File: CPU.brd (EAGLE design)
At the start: 101.6 x 34 mm, 4 parts, among them IC1 Z80CPU

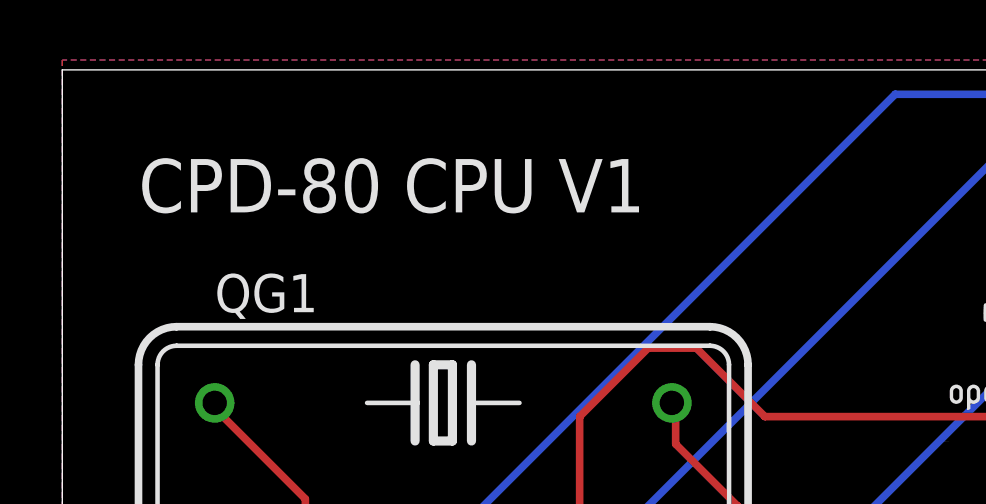
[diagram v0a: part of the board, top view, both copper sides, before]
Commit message: Update names and font
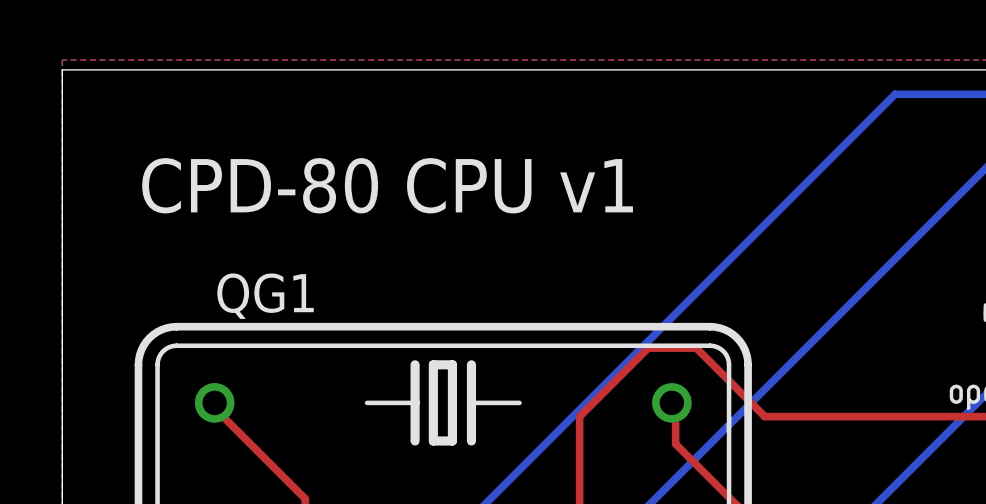
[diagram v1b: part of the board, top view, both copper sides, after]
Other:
- board text added: "CPD-80 CPU v1"
- board text removed: "CPD-80 CPU V1"
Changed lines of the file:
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@@
 <wire x1="102.87" y1="0" x2="102.85" y2="0" width="0.0254" layer="20"/>
 <wire x1="102.85" y1="0" x2="1.27" y2="0" width="0.0254" layer="20"/>
-<text x="3.81" y="29.21" size="1.778" layer="21">CPD-80 CPU V1</text>
+<text x="3.81" y="29.21" size="1.778" layer="21" font="fixed">CPD-80 CPU v1</text>
 <rectangle x1="98.7933" y1="26.7335" x2="99.1235" y2="26.7589" layer="21"/>
 <rectangle x1="98.5901" y1="26.7589" x2="99.1997" y2="26.7843" layer="21"/>

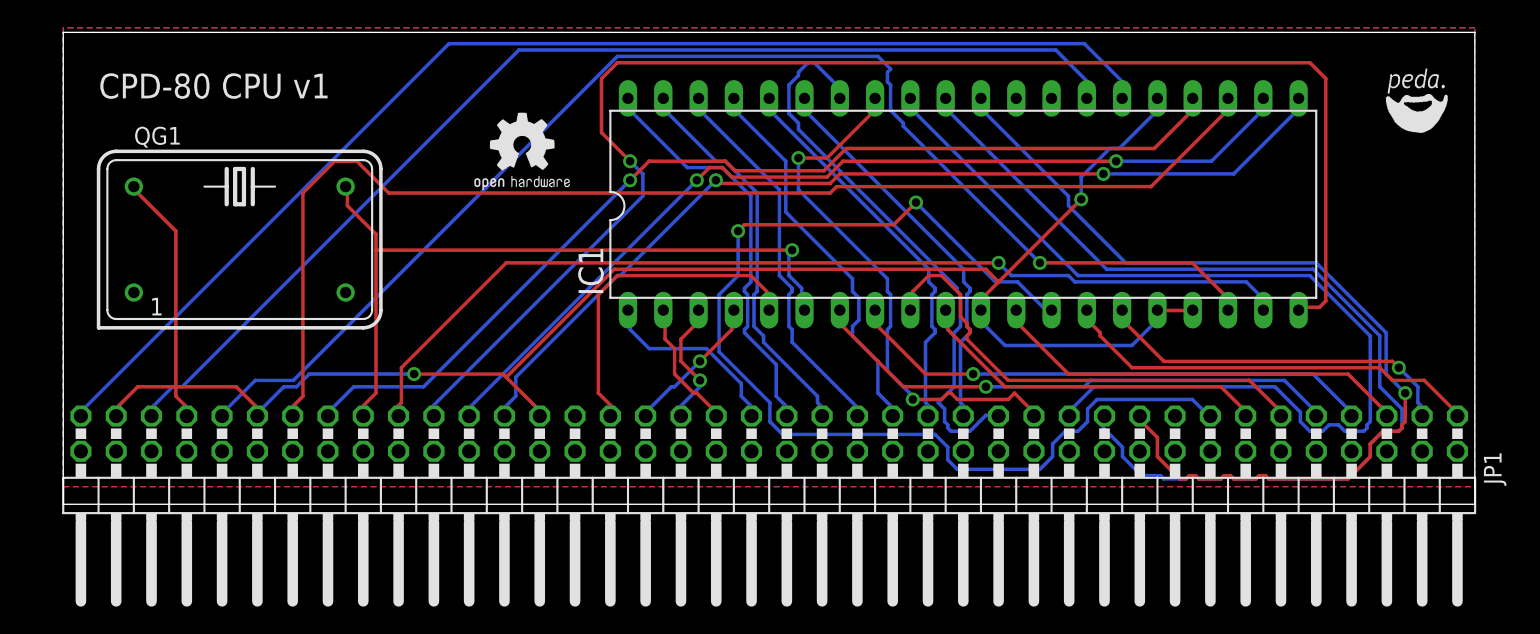
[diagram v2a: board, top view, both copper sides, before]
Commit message: Add Decoupling Capacitors.
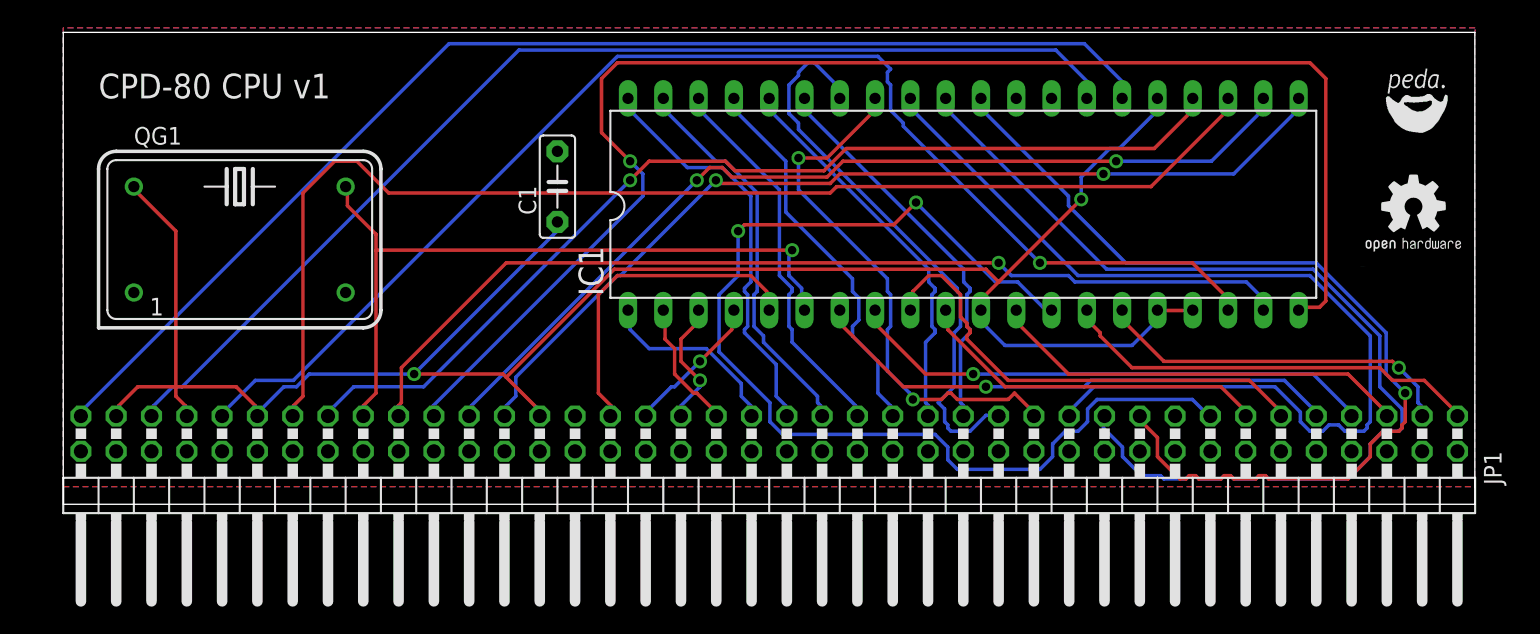
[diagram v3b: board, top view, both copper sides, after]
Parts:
- added C1: 0.1µF, capacitor-wima:C5B2.5
- moved U$1 64.3 mm to (94.6, 17.1)
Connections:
- net GND: now also C1.2
- net VCC: now also C1.1
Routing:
- net VCC: track 132.4 -> 147.6 mm
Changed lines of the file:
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@@
 <attribute name="MF" value="" x="13.97" y="19.05" size="1.778" layer="27" display="off"/>
 </element>
-<element name="U$1" library="bfl" package="OSHW2" value="" x="30.48" y="21.59"/>
+<element name="U$1" library="bfl" package="OSHW2" value="" x="94.615" y="17.145"/>
+<element name="C1" library="capacitor-wima" package="C5B2.5" value="0.1µF" x="36.83" y="22.86" rot="R90"/>
 </elements>
 <signals>
@@
 <via x="74.5236" y="21.9456" extent="1-16" drill="0.6096"/>
 <via x="26.5176" y="9.3726" extent="1-16" drill="0.6096"/>
+<contactref element="C1" pad="1"/>
+<wire x1="36.8046" y1="19.6596" x2="36.8046" y2="20.1168" width="0.254" layer="16"/>
+<wire x1="26.5176" y1="9.3726" x2="36.8046" y2="19.6596" width="0.254" layer="16"/>
+<wire x1="36.8046" y1="20.1168" x2="36.83" y2="20.32" width="0.254" layer="16"/>
 </signal>
 <signal name="GND">
@@
 <vertex x="102.87" y="34.29"/>
 </polygon>
+<contactref element="C1" pad="2"/>
 </signal>
 <signal name="CLOCK">

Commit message: Add Ground Rail to JEANNECTOR
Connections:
- net GND: now also JP1.10, JP1.12, JP1.14, JP1.16, JP1.18, JP1.2, JP1.20, JP1.22, JP1.24, JP1.26, JP1.28, JP1.30, JP1.32, JP1.34, JP1.36, JP1.38, JP1.4, JP1.40, JP1.42, JP1.44, JP1.46, JP1.48, JP1.50, JP1.52, JP1.54, JP1.56, JP1.58, JP1.6, JP1.60, JP1.62, JP1.64, JP1.66, JP1.68, JP1.70, JP1.72, JP1.74, JP1.76, JP1.78, JP1.8, JP1.80
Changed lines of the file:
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@@
 </polygon>
 <contactref element="C1" pad="2"/>
+<contactref element="JP1" pad="2"/>
+<contactref element="JP1" pad="4"/>
+<contactref element="JP1" pad="6"/>
+<contactref element="JP1" pad="8"/>
+<contactref element="JP1" pad="10"/>
+<contactref element="JP1" pad="12"/>
+<contactref element="JP1" pad="14"/>
+<contactref element="JP1" pad="16"/>
+<contactref element="JP1" pad="18"/>
+<contactref element="JP1" pad="20"/>
+<contactref element="JP1" pad="22"/>
+<contactref element="JP1" pad="24"/>
+<contactref element="JP1" pad="26"/>
+<contactref element="JP1" pad="28"/>
+<contactref element="JP1" pad="30"/>
+<contactref element="JP1" pad="32"/>
+<contactref element="JP1" pad="34"/>
+<contactref element="JP1" pad="36"/>
+<contactref element="JP1" pad="38"/>
+<contactref element="JP1" pad="40"/>
+<contactref element="JP1" pad="42"/>
+<contactref element="JP1" pad="44"/>
+<contactref element="JP1" pad="46"/>
+<contactref element="JP1" pad="48"/>
+<contactref element="JP1" pad="50"/>
+<contactref element="JP1" pad="52"/>
+<contactref element="JP1" pad="54"/>
+<contactref element="JP1" pad="56"/>
+<contactref element="JP1" pad="58"/>
+<contactref element="JP1" pad="60"/>
+<contactref element="JP1" pad="62"/>
+<contactref element="JP1" pad="64"/>
+<contactref element="JP1" pad="66"/>
+<contactref element="JP1" pad="68"/>
+<contactref element="JP1" pad="70"/>
+<contactref element="JP1" pad="72"/>
+<contactref element="JP1" pad="74"/>
+<contactref element="JP1" pad="76"/>
+<contactref element="JP1" pad="78"/>
+<contactref element="JP1" pad="80"/>
 </signal>
 <signal name="CLOCK">

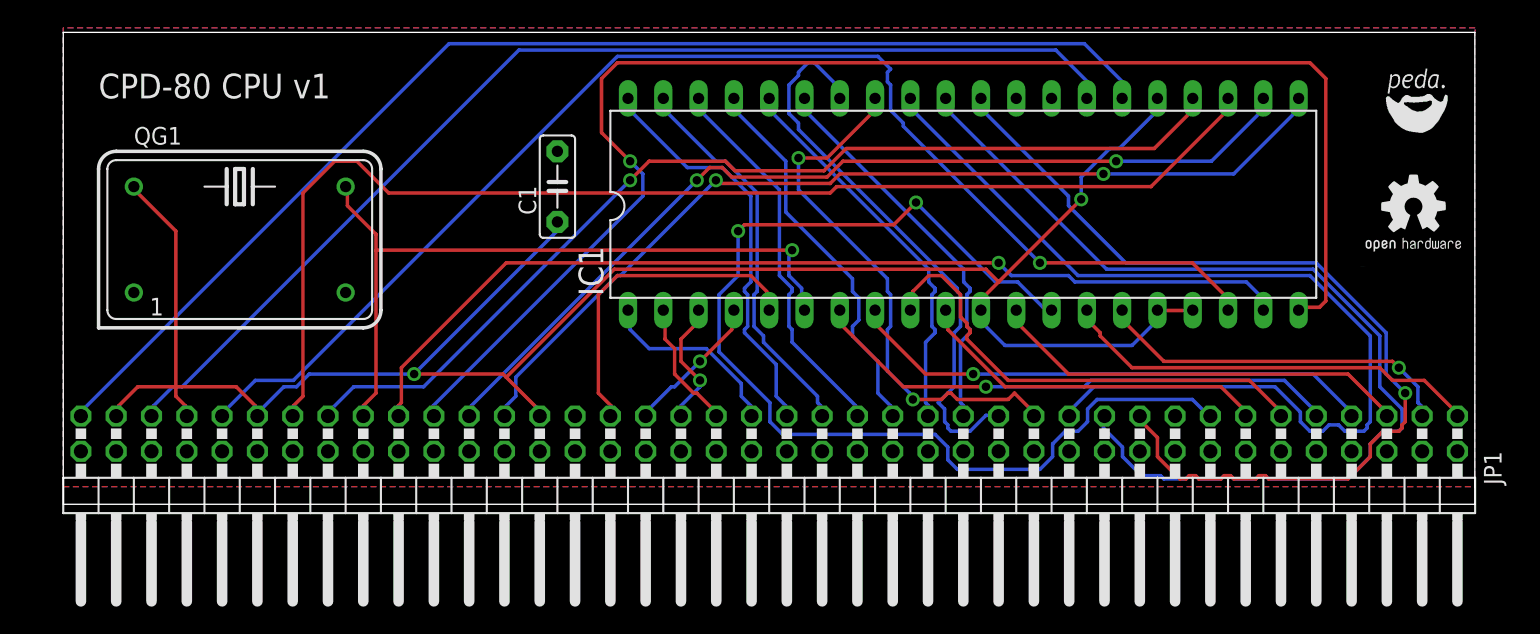
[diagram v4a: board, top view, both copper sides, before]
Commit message: Make Top Plane a VCC Plane instead of Ground, add Holes
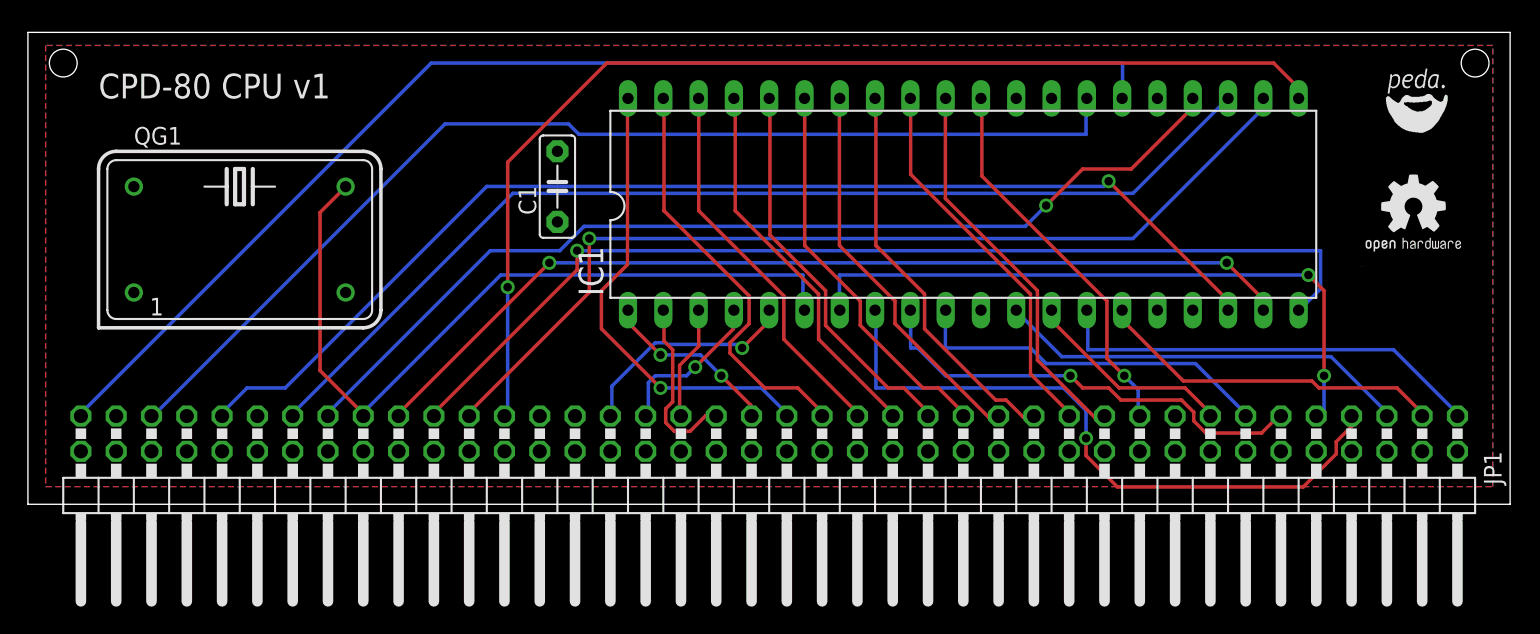
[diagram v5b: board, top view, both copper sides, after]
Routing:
- net VCC: track 147.6 -> 0.00 mm, vias 2 -> 0
- net D7: track 79.7 -> 15.2 mm, vias 2 -> 0
- net A1: track 72.9 -> 28.2 mm
- net A2: track 72.1 -> 27.6 mm
- net A0: track 68.9 -> 27.6 mm
- net N$16: track 103.1 -> 74.6 mm
- net A4: track 41.0 -> 28.2 mm
- net N$14: track 68.4 -> 79.8 mm, vias 2 -> 1
- net N$22: track 88.1 -> 76.9 mm
- net A3: track 39.1 -> 28.6 mm, vias 2 -> 0
- net N$9: track 93.5 -> 83.8 mm
- net D3: track 38.5 -> 47.8 mm
- net D4: track 38.5 -> 47.4 mm, vias 1 -> 2
- net A15: track 23.7 -> 16.6 mm, vias 0 -> 1
- net CLOCK: track 52.7 -> 57.2 mm, vias 1 -> 0
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- added copper zone on layer 1, net VCC
- removed copper zone on layer 1, net GND
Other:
- board size 101.6 x 34 mm -> 106.7 x 34 mm

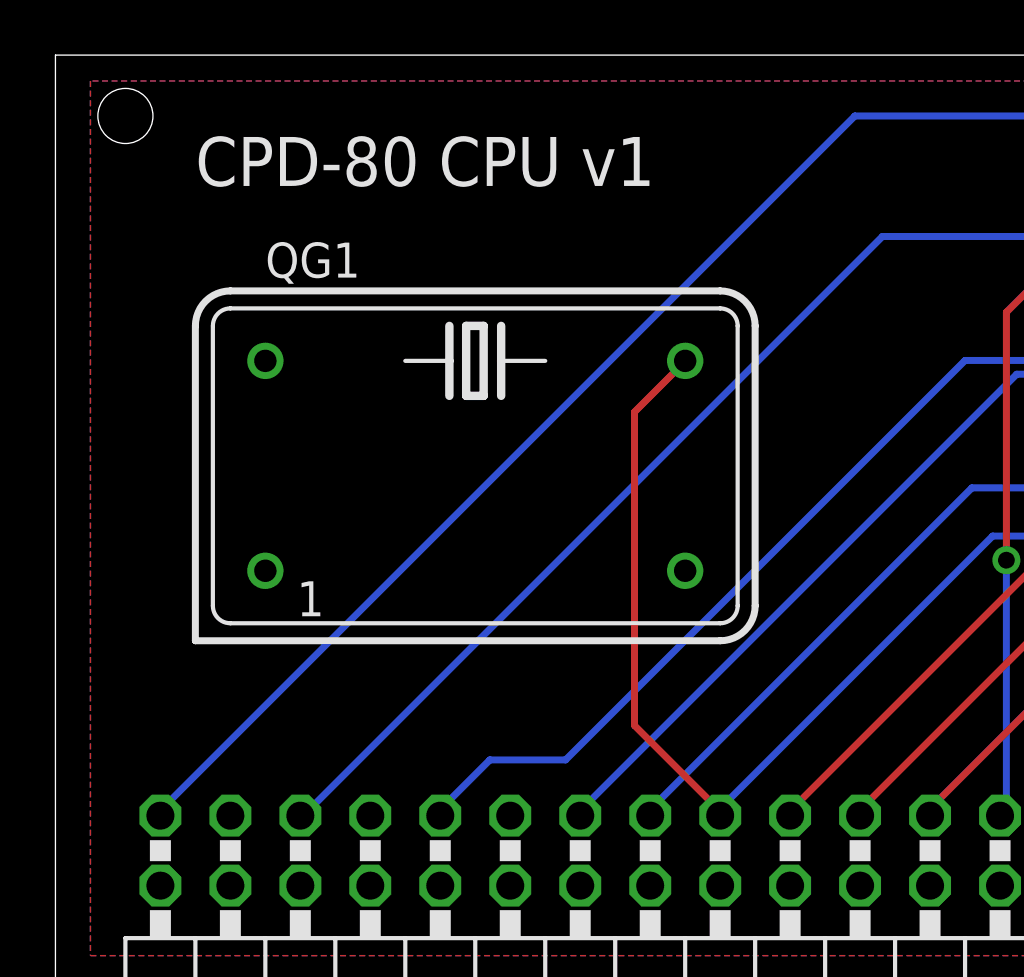
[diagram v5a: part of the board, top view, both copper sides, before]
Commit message: Add PullUp to reset of cpu
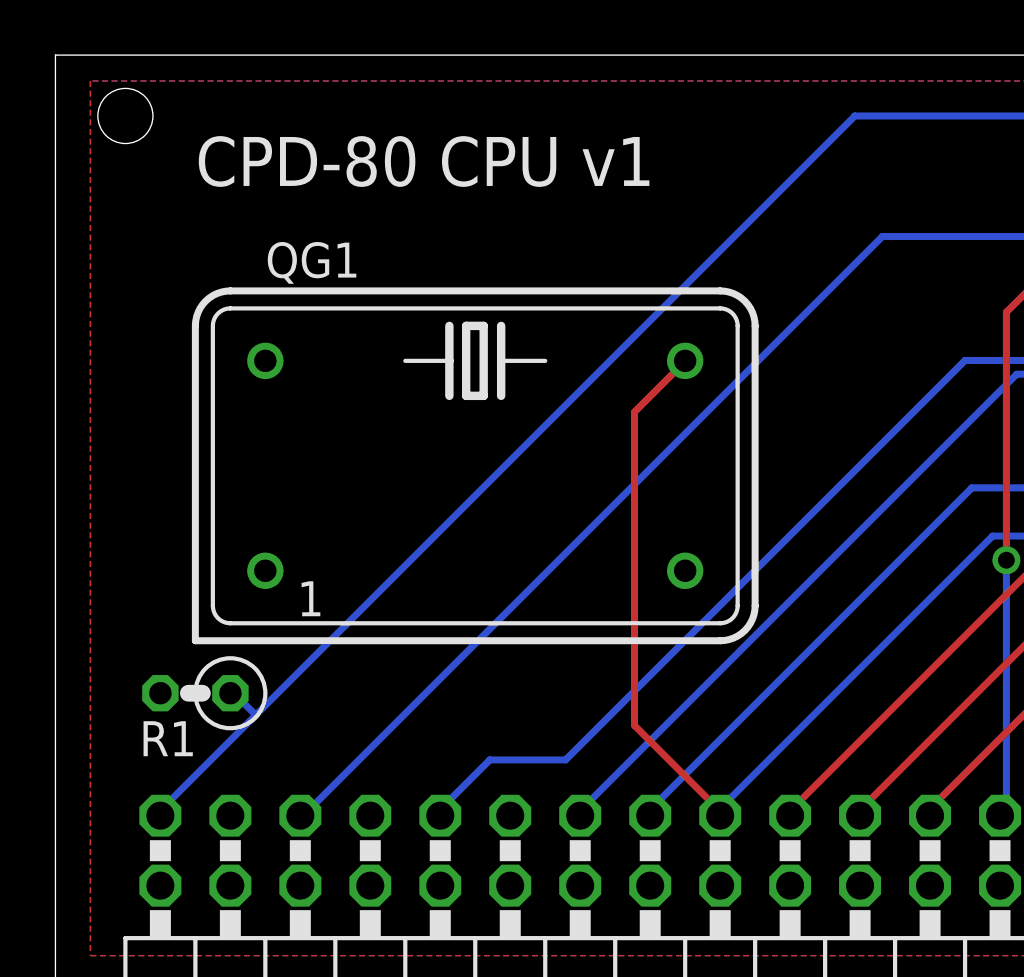
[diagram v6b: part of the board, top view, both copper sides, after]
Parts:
- added R1: 3.3k, resistor:0207/2V
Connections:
- net !RESET: now also R1.1
- net VCC: now also R1.2
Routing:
- net !RESET: track 88.2 -> 89.4 mm
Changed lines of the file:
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@@
 <element name="U$1" library="bfl" package="OSHW2" value="" x="94.615" y="17.145"/>
 <element name="C1" library="capacitor-wima" package="C5B2.5" value="0.1µF" x="36.83" y="22.86" rot="R90"/>
+<element name="R1" library="resistor" package="0207/2V" value="3.3k" x="3.81" y="10.795" rot="R180"/>
 </elements>
 <signals>
@@
 <vertex x="104.14" y="33.02"/>
 </polygon>
+<contactref element="R1" pad="2"/>
 </signal>
 <signal name="GND">
@@
 <wire x1="77.5" y1="31.75" x2="77.5" y2="29.25" width="0.254" layer="16"/>
 <wire x1="27.75" y1="31.75" x2="77.5" y2="31.75" width="0.254" layer="16"/>
-<wire x1="2.625" y1="6.625" x2="27.75" y2="31.75" width="0.254" layer="16"/>
+<wire x1="2.625" y1="6.625" x2="6.001" y2="10.001" width="0.254" layer="16"/>
+<wire x1="6.001" y1="10.001" x2="27.75" y2="31.75" width="0.254" layer="16"/>
 <wire x1="2.625" y1="6.375" x2="2.625" y2="6.625" width="0.254" layer="16"/>
 <wire x1="77.5" y1="29.25" x2="77.47" y2="29.21" width="0.254" layer="16"/>
 <wire x1="2.625" y1="6.375" x2="2.54" y2="6.35" width="0.254" layer="16"/>
+<contactref element="R1" pad="1"/>
+<wire x1="6.001" y1="10.001" x2="5.2578" y2="10.7442" width="0.254" layer="16"/>
+<wire x1="5.2578" y1="10.7442" x2="5.08" y2="10.795" width="0.254" layer="16"/>
 </signal>
 <signal name="WAIT">
